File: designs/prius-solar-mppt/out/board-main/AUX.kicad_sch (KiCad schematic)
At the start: 33 parts, among them U601 LM5164-Q1, U602 LM5164-Q1

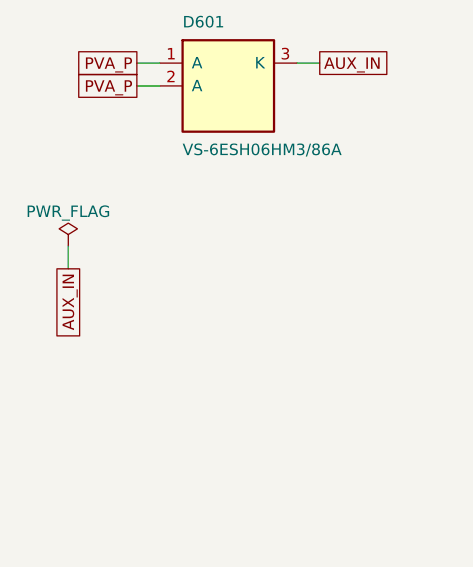
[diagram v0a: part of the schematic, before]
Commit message: designs/prius-solar-mppt: v0.3, fix the independent review's blockers and majors
- B1: CHASSIS domain with reinforced DC barriers to HV and PACK (10/8 mm), HV/PACK edge
  clearance 10 mm, mounting holes fixed with 13 mm keep-outs; thermal pedestal under LV
  parts only.
- B2: no primary source for the Prime's full-charge cell voltage was found (blocking
  Q-13); hardware clamp set below a 4.00 V/cell floor (L3 3.927 V, worst 3.963 V; L2
  3.836 V; L1 3.79 V) with DNP trim to raise later; until then charging may stop near
  55-65 % SOC.
- Majors: sink clamp + burst disable + PV-node trip and TVS against LM5176 reverse power;
  20 MHz AEC-Q200 crystal for CAN (listen-only start); parked insulation monitoring via a
  110 M bridge (also detects a welded relay); open-sensor-safe hardware OT; CAGE CLAMP HV
  terminals with a lid-switch HVIL; DCX on-time and 17.6 A primary overcurrent latches;
  supercap-held latch that clears overnight.
- Build: 0 errors, ERC clean, system and both board netlists identical; 9 waivers (17
  findings, was 32).

Co-Authored-By: Claude Opus 5.5 <noreply@anthropic.com>
Claude-Session: https://claude.ai/code/session_01VFJn9VbX8h27kf4LpLwEtn
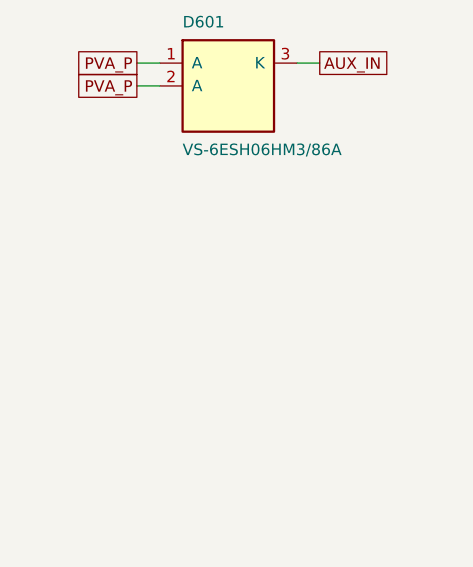
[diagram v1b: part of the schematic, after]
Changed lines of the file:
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@@
-		)
-	)
-	(symbol
-		(lib_id "power:PWR_FLAG")
-		(at 27.94 53.34 0)
-		(unit 1)
-		(exclude_from_sim no)
-		(in_bom no)
-		(on_board yes)
-		(dnp no)
-		(property "Reference" "#FLG15"
-			(at 27.94 51.435 0)
-			(hide yes)
-			(effects
-				(font (size 1.27 1.27))
-			)
-		)
-		(property "Value" "PWR_FLAG"
-			(at 27.94 49.53 0)
-			(effects
-				(font (size 1.27 1.27))
-			)
-		)
-		(property "Footprint" ""
-			(at 27.94 53.34 0)
-			(hide yes)
-			(effects
-				(font (size 1.27 1.27))
-			)
-		)
-		(pin "1"
-		)
-		(instances
-			(project "prius-solar-mppt-main"
-				(path "/16402896-f022-5f91-bcbc-821eea1e3f53/701c6345-fdb4-58aa-8e4b-35889fa36e63"
-					(reference "#FLG15")
-					(unit 1)
-				)
-			)
-		)
-	)
-	(wire
-		(pts (xy 27.94 53.34) (xy 27.94 55.88))
-		(stroke
-			(width 0)
-			(type default)
-		)
-	)
-	(global_label "AUX_IN"
-		(shape passive)
-		(at 27.94 55.88 270)
-		(fields_autoplaced yes)
-		(effects
-			(font (size 1.27 1.27))
-			(justify right)
-		)
-		(property "Intersheetrefs" "${INTERSHEET_REFS}"
-			(at 27.94 55.88 0)
-			(hide yes)
-			(effects
-				(font (size 1.27 1.27))
-			)
 		)
 	)
